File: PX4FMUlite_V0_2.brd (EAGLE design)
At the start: 49.1 x 34.9 mm, 162 parts, among them J201 DF13C-6P-1.25V, J202 DF13C-6P-1.25V, J203 DF13C-6P-1.25V, J204 DF13C-6P-1.25V, J301 47346-0001, J302 DF13C-4P-1.25V, J401 DF13C-4P-1.25V, J403 DF13C-7P-1.25V, J404 DF13C-5P-1.25V, J405 DF13C-4P-1.25V, J702 DF13C-3P-1.25V, J801 JST-ZH-3, M3_MOUNT1101 MOUNT-HOLE3.1MM, M3_MOUNT1102 MOUNT-HOLE3.1MM, M3_MOUNT1103 MOUNT-HOLE3.1MM, M3_MOUNT1104 MOUNT-HOLE3.1MM, U1 MPU-6000QFN-24, U101 STM32F4X7VX, U102 FM25V01, U301 2908-05WB-MG, U401 MAX3051, U701 TCA62724FMG, U703 LRTB GFTG-T7AW-1+V7A7-29+R5T9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, U903 74LVC2G240, X101 3.2x2.5 mm / 24 MHz / 15 ppm

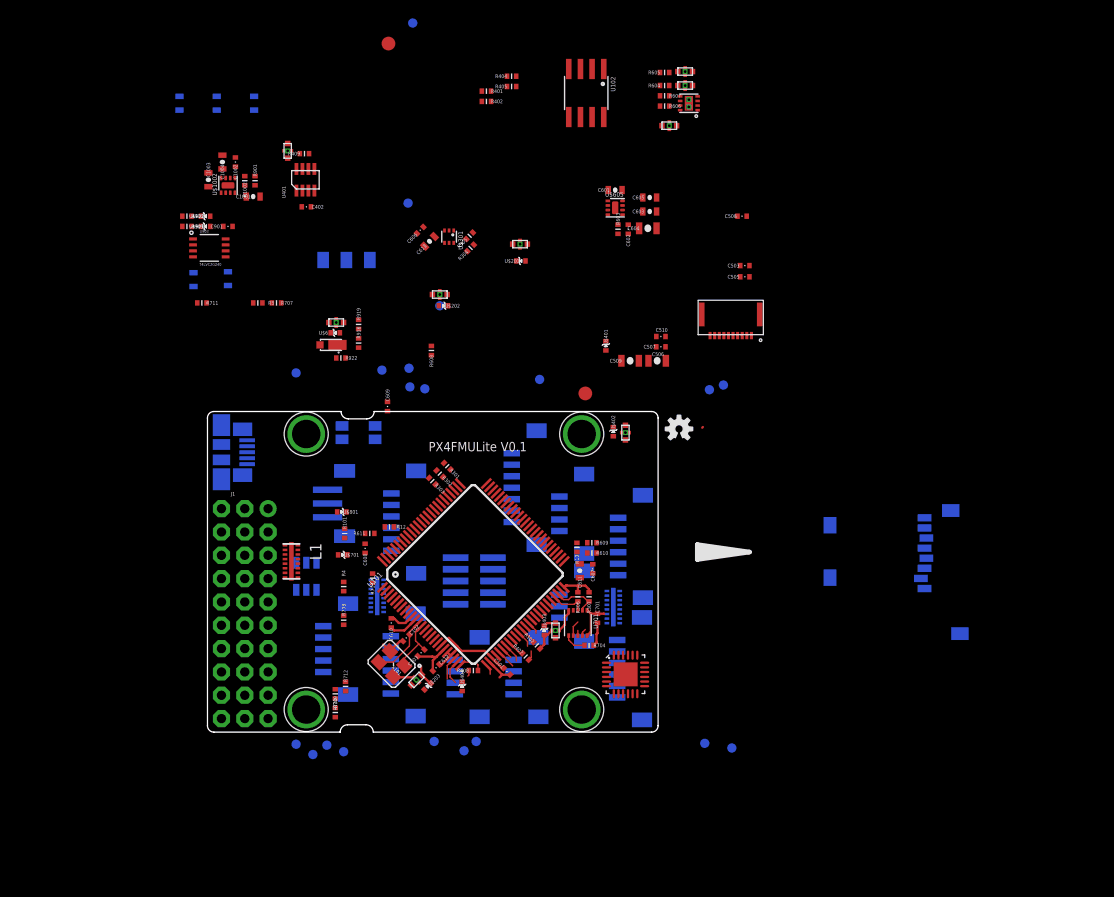
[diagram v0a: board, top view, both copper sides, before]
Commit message: Added V0_2 because V0_1 would not save
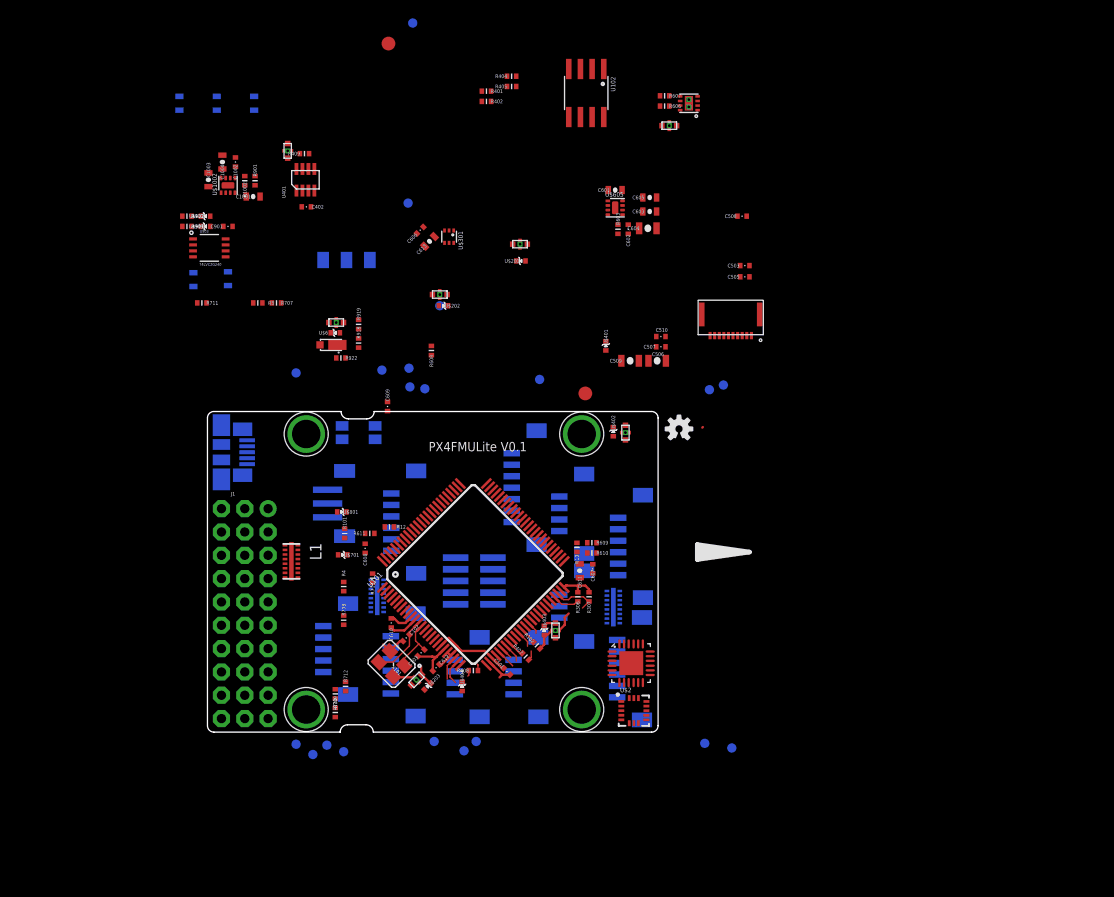
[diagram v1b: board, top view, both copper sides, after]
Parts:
- removed C701: 0u1, pixhawk2:0402-CAP
- removed L601, L602: KNH16C104DA5TS, pixhawk2:KYOCERA-KNH16-DA
- removed R301, R302, R303, R304, R305: 100K, pixhawk2:0402-RES
- removed R604, R605: 10K/0.1%, pixhawk2:0402-RES
- removed R704: 10K, pixhawk2:0402-RES
- removed U301: 2908-05WB-MG, baseboard:MICROSD
- removed U701: TCA62724FMG, pixhawk2:SON10
- removed U703: LRTB GFTG-T7AW-1+V7A7-29+R5T9-49-L, pixhawk2:6-PLCC
- added U$2: LSM303D, PX4FMUlite_V0_1:LGA-16L
- moved U1 1.36 mm to (55.4, 10.3)
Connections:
- removed net BATT_CURRENT_SENS: R604.P$1
- removed net BATT_VOLTAGE_SENS: R605.P$1
- removed net BATT_VOLTAGE_SENS_PROT: L602.P$1
- removed net N$102: L602.P$2, R605.P$2
- removed net N$103: L601.P$2, R604.P$2
- removed net N$21: L601.P$1
- removed net N$95: R704.P$2, U701.6
- removed net RGB_LED_14: U701.7, U703.C3
- removed net RGB_LED_3: U701.9, U703.C1
- removed net RGB_LED_4: U701.8, U703.C2
- net !ACCEL_MAG_CS: now also U$2.8
- net ACCEL_DRDY: now also U$2.11
- net FMU-!RESET: no longer U701.4
- net FMU-I2C2_SCL: no longer U701.3
- net FMU-I2C2_SDA: no longer U701.2
- net FMU-VDD_3V3: no longer C701.P$1, R301.P$2, R302.P$2, R303.P$2, R304.P$2, R305.P$2, U301.4, U701.1, U701.10
- net GNDX: now also U$2.10, U$2.12, U$2.13, U$2.16, U$2.5; no longer C701.P$2, L601.P$3, L601.P$4, L601.P$5, L602.P$3, L602.P$4, L602.P$5, R704.P$1, U301.6, U701.5
- net MAG_DRDY: now also U$2.9
- net N$10: now also U$2.2
- net N$17: now also U$2.3
- net N$6: now also U$2.15
- net SDIO_CK: no longer U301.5
- net SDIO_CMD: no longer R303.P$1, U301.3
- net SDIO_D0: no longer R304.P$1, U301.7
- net SDIO_D1: no longer R305.P$1, U301.8
- net SDIO_D2: no longer R301.P$1, U301.1
- net SDIO_D3: no longer R302.P$1, U301.2
- net SPI_INT_MISO: now also U$2.7
- net SPI_INT_MOSI: now also U$2.6
- net SPI_INT_SCK: now also U$2.4
- net VDD_3V3_SENSORS: now also U$2.1, U$2.14
- net VDD_5V_IN: no longer U703.A1, U703.A2, U703.A3
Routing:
- net FMU-VDD_3V3: track 24.3 -> 19.8 mm
- net GNDX: track 25.2 -> 22.3 mm
- net N$95: track 2.43 -> 0.00 mm
- net RGB_LED_14: track 1.68 -> 0.00 mm
- net FMU-I2C2_SCL: track 3.96 -> 2.99 mm
- net RGB_LED_3: track 0.79 -> 0.00 mm
- net BATT_VOLTAGE_SENS: track 0.66 -> 0.00 mm
- net RGB_LED_4: track 0.56 -> 0.00 mm
- net BATT_CURRENT_SENS: track 0.56 -> 0.00 mm

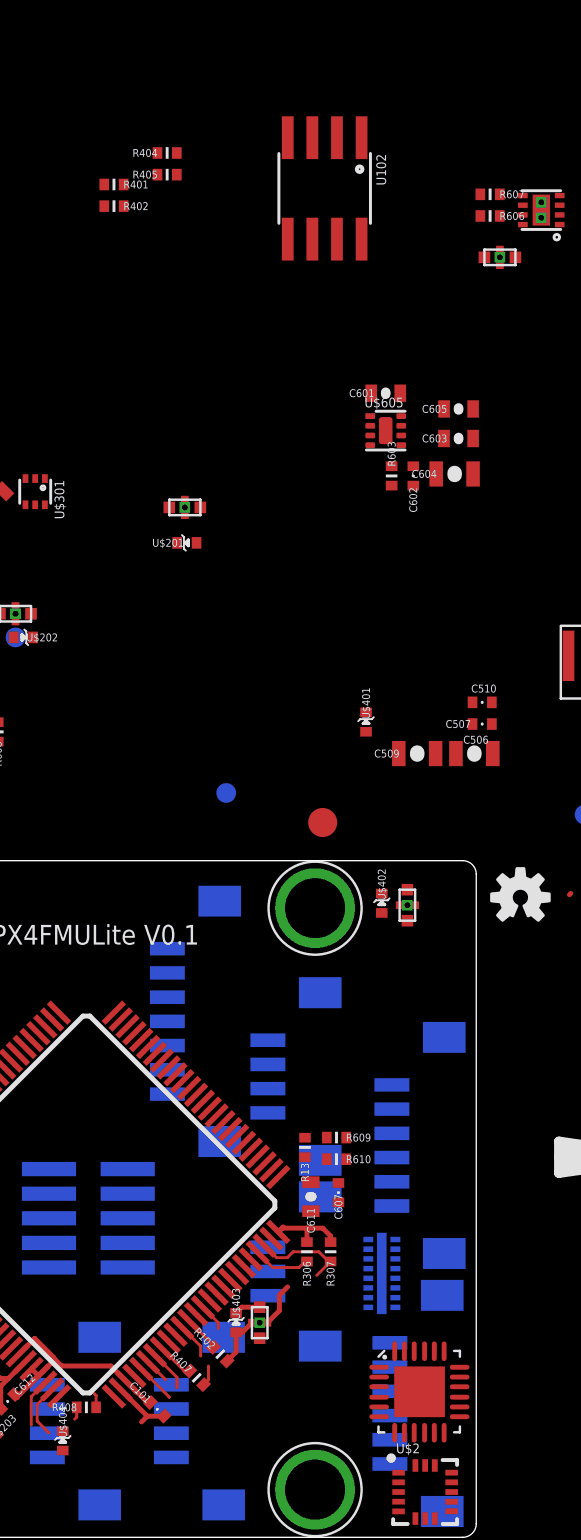
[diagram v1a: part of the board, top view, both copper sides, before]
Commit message: Changed to winbond W25Q64 64mbit flash in 5*6 8WSON
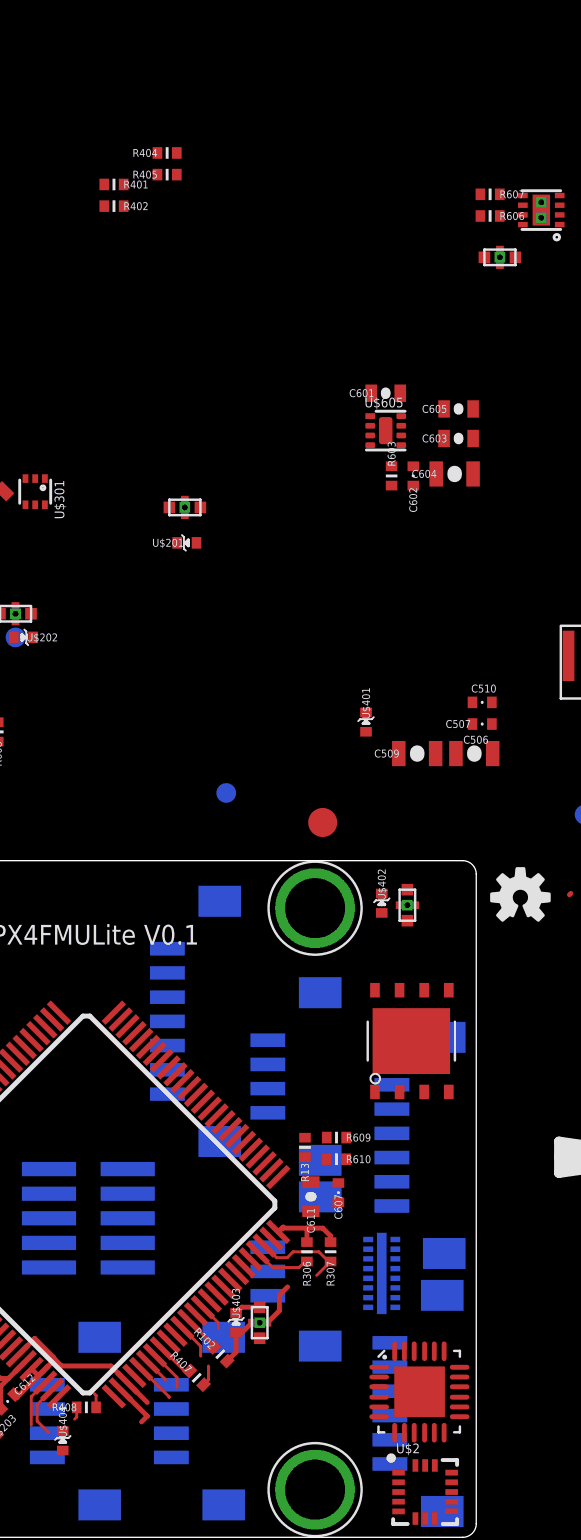
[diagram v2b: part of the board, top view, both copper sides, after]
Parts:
- removed C101: 0u1, pixhawk2:0402-CAP
- removed U102: FM25V01, pixhawk2:SO08
- added U$3: W25Q64FV, PX4lite:WSON-8-5X6
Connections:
- net !FRAM_CS: no longer U102.1
- net FMU-VDD_3V3: no longer C101.P$1, U102.3, U102.7, U102.8
- net FRAM_MISO: no longer U102.2
- net FRAM_MOSI: no longer U102.5
- net FRAM_SCK: no longer U102.6
- net GNDX: no longer C101.P$2, U102.4
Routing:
- net GNDX: track 22.3 -> 21.4 mm
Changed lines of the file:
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@@
 <attribute name="PARTNO" value="RC0402FR-071K5L" x="49.9872" y="17.4752" size="1.778" layer="27" rot="R90" display="off"/>
-</element>
-<element name="U102" library="pixhawk2" package="SO08" value="FM25V01" x="50.4952" y="72.3392" rot="R180">
-<attribute name="MFGPN" value="FM25V01" x="55.7784" y="64.6176" size="1.778" layer="27" rot="R180" display="off"/>
-<attribute name="DATASHEET" value="http://www.ramtron.com/files/datasheets/FM25V01_ds.pdf" x="55.7784" y="64.6176" size="1.778" layer="27" rot="R180" display="off"/>
-<attribute name="LINK" value="http://www.digikey.com/product-detail/en/FM25V01-GTR/1140-1026-1-ND/2809832" x="55.7784" y="64.6176" size="1.778" layer="27" rot="R180" display="off"/>
-<attribute name="PARTNO" value="FM25V01-G" x="50.4952" y="72.3392" size="1.778" layer="27" rot="R180" display="off"/>
-</element>
-<element name="C101" library="pixhawk2" package="0402-CAP" value="0u1" x="41.8592" y="9.3472" rot="R315">
-<attribute name="PARTNO" value="CC0402ZRY5V7BB104" x="41.8592" y="9.3472" size="1.778" layer="27" rot="R315" display="off"/>
 </element>
 <element name="J302" library="con-hirose-df13" package="DF13C-4P-1.25V" value="DF13C-4P-1.25V" x="48.4632" y="26.5176" rot="MR270">
@@
 <attribute name="LINK" value="http://www.st.com/internet/analog/product/253884.jsp" x="55.6768" y="5.08" size="1.778" layer="27" display="off"/>
 </element>
+<element name="U$3" library="PX4lite" package="WSON-8-5X6" value="W25Q64FV" x="54.9656" y="28.3464"/>
 </elements>
 <signals>
@@
 <contactref element="J801" pad="P$2"/>
 <contactref element="R610" pad="P$2"/>
-<contactref element="U102" pad="4"/>
-<contactref element="C101" pad="P$2"/>
 <contactref element="C612" pad="P$2"/>
 <contactref element="U101" pad="20"/>
@@
 <wire x1="32.2112875" y1="10.9728" x2="33.7312" y2="10.9728" width="0.254" layer="1"/>
 <wire x1="39.969365625" y1="10.36765625" x2="41.343378125" y2="8.99364375" width="0.254" layer="1"/>
-<wire x1="41.343378125" y1="8.99364375" x2="42.212753125" y2="8.99364375" width="0.254" layer="1"/>
 <contactref element="J302" pad="P$4"/>
 <contactref element="U$301" pad="2"/>
@@
 <wire x1="21.8584" y1="9.2856" x2="21.8584" y2="11.7856" width="0" layer="19" extent="16-16"/>
 <wire x1="41.0464" y1="8.696665625" x2="36.9824" y2="7.2216" width="0" layer="19" extent="1-1"/>
-<wire x1="42.5848" y1="6.8626" x2="42.212753125" y2="8.99364375" width="0" layer="19" extent="1-16"/>
-<wire x1="45.463953125" y1="11.83844375" x2="42.212753125" y2="8.99364375" width="0" layer="19" extent="1-1"/>
+<wire x1="42.5848" y1="6.8626" x2="41.0464" y2="8.696665625" width="0" layer="19" extent="1-16"/>
+<wire x1="45.463953125" y1="11.83844375" x2="41.343378125" y2="8.99364375" width="0" layer="19" extent="1-1"/>
 <wire x1="53.4416" y1="16.3576" x2="48.5808" y2="15.6624" width="0" layer="19" extent="1-16"/>
 <wire x1="53.964" y1="19.8366" x2="53.4416" y2="16.3576" width="0" layer="19" extent="16-16"/>
@@
 <wire x1="57.0468" y1="4.58" x2="57.0468" y2="5.58" width="0" layer="19" extent="1-1"/>
 <wire x1="54.3068" y1="4.08" x2="53.8624" y2="6.527" width="0" layer="19" extent="1-16"/>
-<wire x1="48.5902" y1="74.9554" x2="58.5296" y2="72.0344" width="0" layer="19" extent="1-1"/>
 </signal>
 <signal name="FMU-VDD_3V3" class="1">
@@
 <contactref element="R307" pad="P$2"/>
 <contactref element="R306" pad="P$2"/>
-<contactref element="U102" pad="8"/>
-<contactref element="C101" pad="P$1"/>
-<contactref element="U102" pad="7"/>
-<contactref element="U102" pad="3"/>
 <contactref element="U101" pad="21"/>
 <contactref element="C612" pad="P$1"/>
@@
 <wire x1="34.759115625" y1="10.107153125" x2="34.491153125" y2="10.107153125" width="0.254" layer="1"/>
 <wire x1="40.32291875" y1="10.721209375" x2="41.343375" y2="9.700753125" width="0.254" layer="1"/>
-<wire x1="41.343375" y1="9.700753125" x2="41.50564375" y2="9.700753125" width="0.254" layer="1"/>
 <wire x1="48.10109375" y1="18.499384375" x2="48.296109375" y2="18.6944" width="0.254" layer="1"/>
 <wire x1="48.296109375" y1="18.6944" x2="49.5808" y2="18.6944" width="0.254" layer="1"/>
@@
 <wire x1="36.576" y1="11.9240375" x2="36.9176375" y2="11.5824" width="0.254" layer="1"/>
 <wire x1="36.9176375" y1="11.5824" x2="39.461728125" y2="11.5824" width="0.254" layer="1"/>
-<wire x1="51.1302" y1="69.723" x2="49.8602" y2="74.9554" width="0" layer="19" extent="1-1"/>
-<wire x1="52.4002" y1="69.723" x2="51.1302" y2="69.723" width="0" layer="19" extent="1-1"/>
-<wire x1="54.4448" y1="60.0924" x2="52.4002" y2="69.723" width="0" layer="19" extent="1-1"/>
-<wire x1="56.654" y1="59.436" x2="54.4448" y2="60.0924" width="0" layer="19" extent="1-1"/>
 <wire x1="56.2508" y1="57.6072" x2="56.654" y2="59.436" width="0" layer="19" extent="1-1"/>
-<wire x1="39.124" y1="72.5424" x2="49.8602" y2="74.9554" width="0" layer="19" extent="1-1"/>
-<wire x1="39.124" y1="71.4248" x2="39.124" y2="72.5424" width="0" layer="19" extent="1-1"/>
+<wire x1="54.4448" y1="60.0924" x2="56.654" y2="59.436" width="0" layer="19" extent="1-1"/>
+<wire x1="39.124" y1="71.4248" x2="54.4448" y2="60.0924" width="0" layer="19" extent="1-1"/>
+<wire x1="39.124" y1="72.5424" x2="39.124" y2="71.4248" width="0" layer="19" extent="1-1"/>
 <wire x1="32.05684375" y1="57.05044375" x2="39.124" y2="71.4248" width="0" layer="19" extent="1-1"/>
 <wire x1="20.5152" y1="59.944" x2="32.05684375" y2="57.05044375" width="0" layer="19" extent="1-1"/>
@@
 </signal>
 <signal name="!FRAM_CS">
-<contactref element="U102" pad="1"/>
 <contactref element="U101" pad="57"/>
-<wire x1="45.979771875" y1="23.44913125" x2="52.4002" y2="74.9554" width="0" layer="19" extent="1-1"/>
 </signal>
 <signal name="FRAM_SCK">
-<contactref element="U102" pad="6"/>
 <contactref element="U101" pad="52"/>
-<wire x1="47.747540625" y1="21.681365625" x2="49.8602" y2="69.723" width="0" layer="19" extent="1-1"/>
 </signal>
 <signal name="FRAM_MOSI">
-<contactref element="U102" pad="5"/>
 <contactref element="U101" pad="54"/>
-<wire x1="47.040434375" y1="22.388471875" x2="48.5902" y2="69.723" width="0" layer="19" extent="1-1"/>
 </signal>
 <signal name="FRAM_MISO">
-<contactref element="U102" pad="2"/>
 <contactref element="U101" pad="53"/>
-<wire x1="47.3939875" y1="22.03491875" x2="51.1302" y2="74.9554" width="0" layer="19" extent="1-1"/>
 </signal>
 <signal name="FMU-SWCLK">

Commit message: Test positioning
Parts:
- moved L403 65.2 mm to (38.8, 4.27), turned to 180 degrees
- moved R409 62.7 mm to (39.1, 6.10), turned to 90 degrees
- moved U401 60.8 mm to (42.0, 6.20), turned to 90 degrees
- moved C402 59.1 mm to (44.9, 6.30), turned to 270 degrees
- moved C1004 54.8 mm to (56.4, 34.3), turned to 0 degrees
- moved C1002 54.4 mm to (56.4, 32.9), turned to 0 degrees
- moved C1003 52.6 mm to (54.5, 35.9), turned to 180 degrees
- moved R1002 51.4 mm to (54.4, 31.9), turned to 0 degrees
- moved R901 51.2 mm to (54.4, 30.8), turned to 180 degrees
- moved U$1002 51.1 mm to (53.8, 33.7), turned to 0 degrees
- moved C1001 48.8 mm to (52.6, 31.0), turned to 270 degrees
- moved C602 34.0 mm to (32.6, 32.0)
- moved C603 34.0 mm to (35.0, 33.9)
- moved C605 34.0 mm to (35.0, 35.5)
- moved C601 34.0 mm to (31.2, 36.3)
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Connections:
- new net GND: U$3.4
- net FMU-VDD_3V3: now also U$3.8
- net SDIO_CK: now also U$3.6
- net SDIO_CMD: now also U$3.1
- net SDIO_D0: now also U$3.5
- net SDIO_D1: now also U$3.2
- net SDIO_D2: now also U$3.3
- net SDIO_D3: now also U$3.7
